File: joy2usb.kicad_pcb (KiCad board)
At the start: 2 copper layers, 55 x 90 mm, 18 parts, among them J1 DB9_Male, J2 Conn_02x04_Odd_Even, SW1 RST, SW2 SW_SPDT, U1 Arduino_Pro_Micro, U2 4066

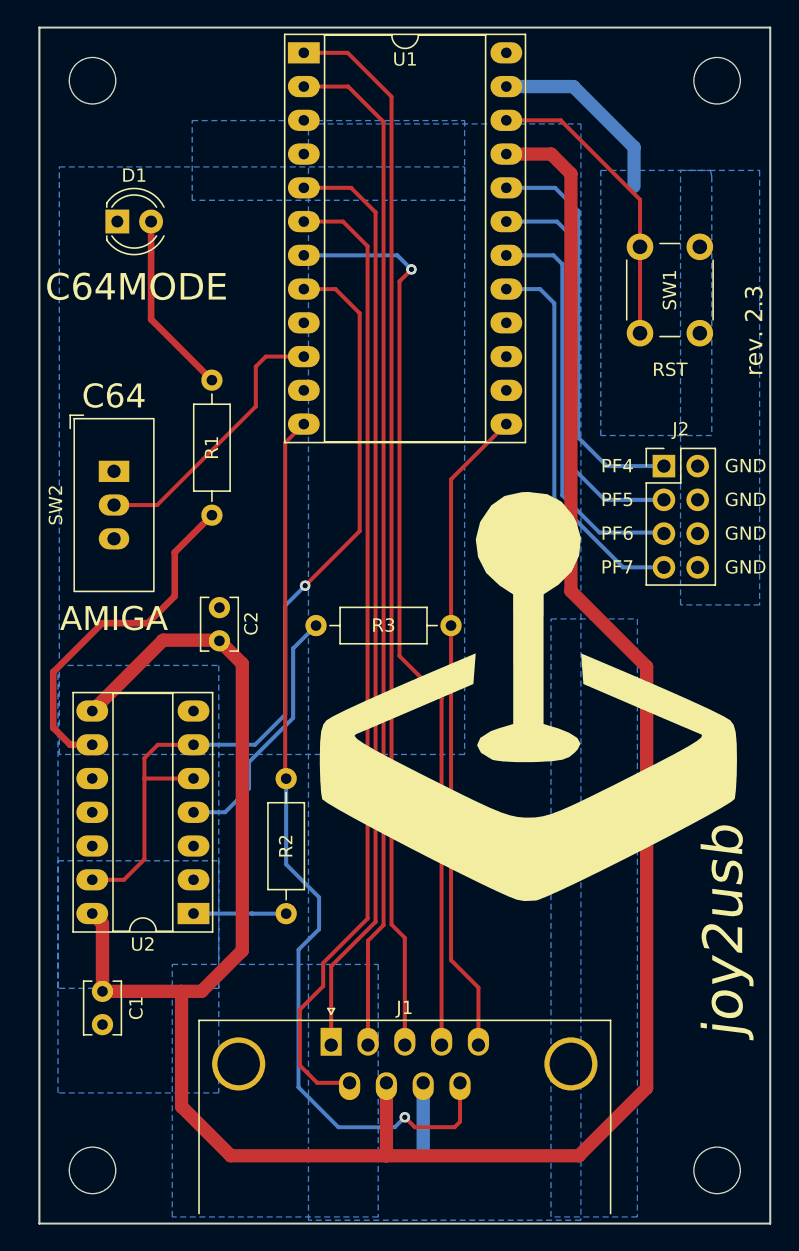
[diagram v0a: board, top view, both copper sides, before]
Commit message: PCB Rev. 2.4
update: rounded corners
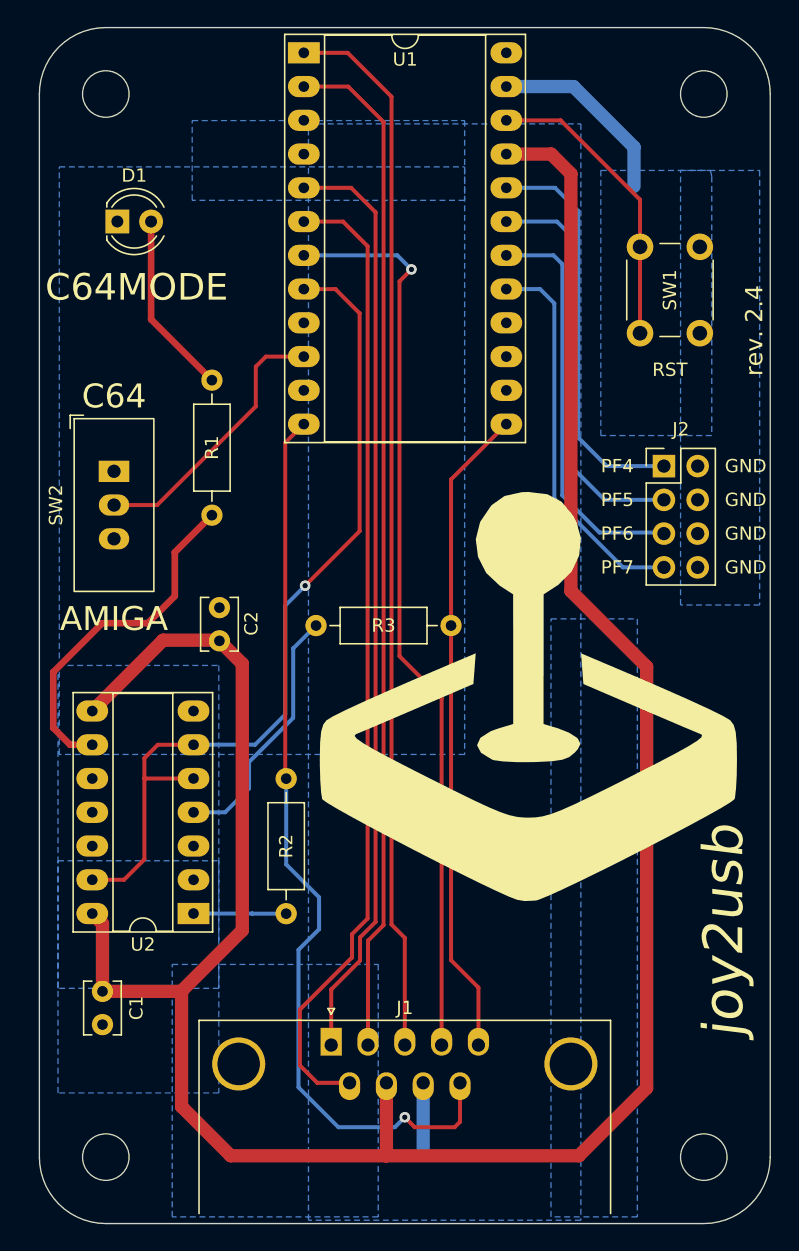
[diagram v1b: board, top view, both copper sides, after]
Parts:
- moved H1 1.41 mm to (118.0, 140.0)
- moved H2 1.41 mm to (163.0, 60.0)
- moved H3 1.41 mm to (118.0, 60.0)
- moved H4 1.41 mm to (163.0, 140.0)
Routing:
- net VCC: track 183.2 -> 182.4 mm
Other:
- outline, holes or cut-outs redrawn
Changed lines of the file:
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@@
   (title_block
     (title "joy2usb")
-    (rev "2.3")
+    (rev "2.4")
     (company "mistepien")
   )
@@
   (net 26 "unconnected-(U1-Pad3)")
   (net 27 "Net-(R1-Pad1)")
-  (net 28 "Net-(R2-Pad2)")
-  (net 29 "Net-(R3-Pad1)")
+  (net 28 "Net-(U2-Pad1)")
+  (net 29 "Net-(U2-Pad4)")
   (footprint "Resistor_THT:R_Axial_DIN0207_L6.3mm_D2.5mm_P10.16mm_Horizontal" (layer "F.Cu")
     (at 133.82 100)
@@
     (fp_line (start 8.23 -1.25) (end 1.93 -1.25) (layer "F.Fab") (width 0.1))
     (pad "1" thru_hole circle (at 0 0) (size 1.6 1.6) (drill 0.8) (layers *.Cu *.Mask)
-      (net 29 "Net-(R3-Pad1)") (pintype "passive"))
+      (net 29 "Net-(U2-Pad4)") (pintype "passive"))
     (pad "2" thru_hole oval (at 10.16 0) (size 1.6 1.6) (drill 0.8) (layers *.Cu *.Mask)
       (net 5 "/F3BTN") (pintype "passive"))
@@
       (net 9 "/F2BTN") (pintype "passive"))
     (pad "2" thru_hole oval (at 10.16 0 270) (size 1.6 1.6) (drill 0.8) (layers *.Cu *.Mask)
-      (net 28 "Net-(R2-Pad2)") (pintype "passive"))
+      (net 28 "Net-(U2-Pad1)") (pintype "passive"))
     (model "${KICAD6_3DMODEL_DIR}/Resistor_THT.3dshapes/R_Axial_DIN0207_L6.3mm_D2.5mm_P10.16mm_Horizontal.wrl"
       (offset (xyz 0 0 0))
@@
   )
   (footprint "MountingHole:MountingHole_3.5mm" (layer "F.Cu")
-    (at 164 141)
+    (at 163 140)
     (descr "Mounting Hole 3.5mm, no annular")
     (tags "mounting hole 3.5mm no annular")
@@
   )
   (footprint "MountingHole:MountingHole_3.5mm" (layer "F.Cu")
-    (at 164 59)
+    (at 163 60)
     (descr "Mounting Hole 3.5mm, no annular")
     (tags "mounting hole 3.5mm no annular")
@@
     (fp_line (start 1.635 -1.27) (end 6.985 -1.27) (layer "F.Fab") (width 0.1))
     (pad "1" thru_hole rect (at 0 0 180) (size 2.4 1.6) (drill 0.8) (layers *.Cu *.Mask)
-      (net 28 "Net-(R2-Pad2)") (pintype "passive"))
+      (net 28 "Net-(U2-Pad1)") (pintype "passive"))
     (pad "2" thru_hole oval (at 0 2.54 180) (size 2.4 1.6) (drill 0.8) (layers *.Cu *.Mask)
       (net 8 "GND1") (pintype "passive"))
@@
       (net 8 "GND1") (pintype "passive"))
     (pad "4" thru_hole oval (at 0 7.62 180) (size 2.4 1.6) (drill 0.8) (layers *.Cu *.Mask)
-      (net 29 "Net-(R3-Pad1)") (pintype "passive"))
+      (net 29 "Net-(U2-Pad4)") (pintype "passive"))
     (pad "5" thru_hole oval (at 0 10.16 180) (size 2.4 1.6) (drill 0.8) (layers *.Cu *.Mask)
       (net 24 "/F2F3MODE") (pintype "input"))
@@
   )
   (footprint "MountingHole:MountingHole_3.5mm" (layer "F.Cu")
-    (at 117 59)
+    (at 118 60)
     (descr "Mounting Hole 3.5mm, no annular")
     (tags "mounting hole 3.5mm no annular")
@@
   )
   (footprint "MountingHole:MountingHole_3.5mm" (layer "F.Cu")
-    (at 117 141)
+    (at 118 140)
     (descr "Mounting Hole 3.5mm, no annular")
     (tags "mounting hole 3.5mm no annular")
@@
       ) (layer "B.SilkS") (width 0.01) (fill solid))
   )
-  (gr_rect (start 113 55) (end 168 145) (layer "Edge.Cuts") (width 0.15) (fill none))
+  (gr_line (start 163 55) (end 118 55) (layer "Edge.Cuts") (width 0.1))
+  (gr_line (start 118 145) (end 163 145) (layer "Edge.Cuts") (width 0.1))
+  (gr_arc (start 163 55) (mid 166.535534 56.464466) (end 168 60) (layer "Edge.Cuts") (width 0.1))
+  (gr_arc (start 113 60) (mid 114.464466 56.464466) (end 118 55) (layer "Edge.Cuts") (width 0.1))
+  (gr_line (start 168 140) (end 168 60) (layer "Edge.Cuts") (width 0.1))
+  (gr_arc (start 168 140) (mid 166.535534 143.535534) (end 163 145) (layer "Edge.Cuts") (width 0.1))
+  (gr_arc (start 118 145) (mid 114.464466 143.535534) (end 113 140) (layer "Edge.Cuts") (width 0.1))
+  (gr_line (start 113 60) (end 113 140) (layer "Edge.Cuts") (width 0.1))
   (gr_text "rev. ${REVISION}" (at 166.8 71.5 -90) (layer "B.SilkS")
     (effects (font (size 1.3 1.3) (thickness 0.3)) (justify mirror))
@@
   )
   (dimension (type aligned) (layer "Dwgs.User")
-    (pts (xy 164 141) (xy 164 59))
+    (pts (xy 163 140) (xy 163 60))
     (height 22.5)
-    (gr_text "82.0000 mm" (at 185.35 100 90) (layer "Dwgs.User")
+    (gr_text "80.0000 mm" (at 184.35 100 90) (layer "Dwgs.User")
       (effects (font (size 1 1) (thickness 0.15)))
     )
@@
   )
   (dimension (type aligned) (layer "Dwgs.User")
-    (pts (xy 117 59) (xy 164 59))
+    (pts (xy 118 60) (xy 163 60))
     (height -27)
-    (gr_text "47.0000 mm" (at 140.5 30.85) (layer "Dwgs.User")
+    (gr_text "45.0000 mm" (at 140.5 31.85) (layer "Dwgs.User")
       (effects (font (size 1 1) (thickness 0.15)))
     )
@@
   )
   (dimension (type aligned) (layer "Dwgs.User")
-    (pts (xy 113 55) (xy 168 55))
-    (height -13.8)
-    (gr_text "55.0000 mm" (at 140.5 40.05) (layer "Dwgs.User")
+    (pts (xy 113 60) (xy 168 60))
+    (height -20)
+    (gr_text "55.0000 mm" (at 140.5 38.85) (layer "Dwgs.User")
       (effects (font (size 1 1) (thickness 0.15)))
     )
@@
   )
   (dimension (type aligned) (layer "Dwgs.User")
-    (pts (xy 168 55) (xy 168 145))
-    (height -6.5)
-    (gr_text "90.0000 mm" (at 173.35 100 90) (layer "Dwgs.User")
+    (pts (xy 163 55) (xy 163 145))
+    (height -16)
+    (gr_text "90.0000 mm" (at 177.85 100 90) (layer "Dwgs.User")
       (effects (font (size 1 1) (thickness 0.15)))
     )
@@
     (style (thickness 0.15) (arrow_length 1.27) (text_position_mode 0) (extension_height 0.58642) (extension_offset 0.5) keep_text_aligned)
   )
+  (segment (start 136.46 67.06) (end 138.3 68.9) (width 0.3) (layer "F.Cu") (net 1))
+  (segment (start 137.13 125.218528) (end 134.96 127.388528) (width 0.3) (layer "F.Cu") (net 1))
   (segment (start 132.9 67.06) (end 136.46 67.06) (width 0.3) (layer "F.Cu") (net 1))
-  (segment (start 136.46 67.06) (end 138.3 68.9) (width 0.3) (layer "F.Cu") (net 1))
-  (segment (start 134.96 125.638528) (end 134.96 131.569669) (width 0.3) (layer "F.Cu") (net 1))
-  (segment (start 138.3 122.298528) (end 134.96 125.638528) (width 0.3) (layer "F.Cu") (net 1))
   (segment (start 138.3 68.9) (end 138.3 122.298528) (width 0.3) (layer "F.Cu") (net 1))
+  (segment (start 134.96 127.388528) (end 134.96 131.569669) (width 0.3) (layer "F.Cu") (net 1))
+  (segment (start 137.13 123.468528) (end 137.13 125.218528) (width 0.3) (layer "F.Cu") (net 1))
+  (segment (start 138.3 122.298528) (end 137.13 123.468528) (width 0.3) (layer "F.Cu") (net 1))
   (segment (start 132.9 59.44) (end 136.24 59.44) (width 0.3) (layer "F.Cu") (net 2))
   (segment (start 137.73 123.717056) (end 137.73 131.569669) (width 0.3) (layer "F.Cu") (net 2))
@@
   (segment (start 146.04 127.24) (end 146.04 131.569669) (width 0.3) (layer "F.Cu") (net 5))
   (segment (start 143.98 100) (end 143.98 125.18) (width 0.3) (layer "F.Cu") (net 5))
+  (segment (start 136.53 124.97) (end 132.6 128.9) (width 0.3) (layer "F.Cu") (net 6))
+  (segment (start 137.7 122.05) (end 136.53 123.22) (width 0.3) (layer "F.Cu") (net 6))
+  (segment (start 136.53 123.22) (end 136.53 124.97) (width 0.3) (layer "F.Cu") (net 6))
   (segment (start 137.7 71.45) (end 137.7 122.05) (width 0.3) (layer "F.Cu") (net 6))
-  (segment (start 137.7 122.05) (end 134.36 125.39) (width 0.3) (layer "F.Cu") (net 6))
-  (segment (start 135.85 69.6) (end 137.7 71.45) (width 0.3) (layer "F.Cu") (net 6))
-  (segment (start 134.36 127.14) (end 132.6 128.9) (width 0.3) (layer "F.Cu") (net 6))
+  (segment (start 133.909669 134.409669) (end 136.345 134.409669) (width 0.3) (layer "F.Cu") (net 6))
+  (segment (start 132.6 133.1) (end 133.909669 134.409669) (width 0.3) (layer "F.Cu") (net 6))
   (segment (start 132.6 128.9) (end 132.6 133.1) (width 0.3) (layer "F.Cu") (net 6))
   (segment (start 132.9 69.6) (end 135.85 69.6) (width 0.3) (layer "F.Cu") (net 6))
-  (segment (start 132.6 133.1) (end 133.909669 134.409669) (width 0.3) (layer "F.Cu") (net 6))
-  (segment (start 134.36 125.39) (end 134.36 127.14) (width 0.3) (layer "F.Cu") (net 6))
-  (segment (start 133.909669 134.409669) (end 136.345 134.409669) (width 0.3) (layer "F.Cu") (net 6))
-  (segment (start 128.27 124.46) (end 125.202 127.528) (width 1) (layer "F.Cu") (net 7))
+  (segment (start 135.85 69.6) (end 137.7 71.45) (width 0.3) (layer "F.Cu") (net 6))
   (segment (start 158.7 134.8) (end 153.6 139.9) (width 1) (layer "F.Cu") (net 7))
   (segment (start 123.7 136.2) (end 127.4 139.9) (width 1) (layer "F.Cu") (net 7))
   (segment (start 117.75 127.528) (end 117.75 122.441) (width 1) (layer "F.Cu") (net 7))
-  (segment (start 122.311 101.1) (end 126.5 101.1) (width 1) (layer "F.Cu") (net 7))
   (segment (start 117.75 122.441) (end 116.98 121.671) (width 1) (layer "F.Cu") (net 7))
   (segment (start 158.7 103.1) (end 158.7 134.8) (width 1) (layer "F.Cu") (net 7))
+  (segment (start 122.311 101.1) (end 126.5 101.1) (width 1) (layer "F.Cu") (net 7))
   (segment (start 126.5 101.1) (end 128.27 102.87) (width 1) (layer "F.Cu") (net 7))
   (segment (start 139.115 139.885) (end 139.1 139.9) (width 1) (layer "F.Cu") (net 7))
@@
   (segment (start 139.115 134.409669) (end 139.115 139.885) (width 1) (layer "F.Cu") (net 7))
   (segment (start 123.7 136.2) (end 123.7 127.55) (width 1) (layer "F.Cu") (net 7))
-  (segment (start 128.27 102.87) (end 128.27 124.46) (width 1) (layer "F.Cu") (net 7))
+  (segment (start 128.27 122.936) (end 123.678 127.528) (width 1) (layer "F.Cu") (net 7))
   (segment (start 153 66) (end 153 97.4) (width 1) (layer "F.Cu") (net 7))
   (segment (start 117.75 127.528) (end 123.678 127.528) (width 1) (layer "F.Cu") (net 7))
   (segment (start 153.6 139.9) (end 139.1 139.9) (width 1) (layer "F.Cu") (net 7))
-  (segment (start 125.202 127.528) (end 123.678 127.528) (width 1) (layer "F.Cu") (net 7))
   (segment (start 127.4 139.9) (end 139.1 139.9) (width 1) (layer "F.Cu") (net 7))
+  (segment (start 128.27 102.87) (end 128.27 122.936) (width 1) (layer "F.Cu") (net 7))
   (segment (start 123.7 127.55) (end 123.678 127.528) (width 1) (layer "F.Cu") (net 7))
   (segment (start 151.52 64.52) (end 153 66) (width 1) (layer "F.Cu") (net 7))

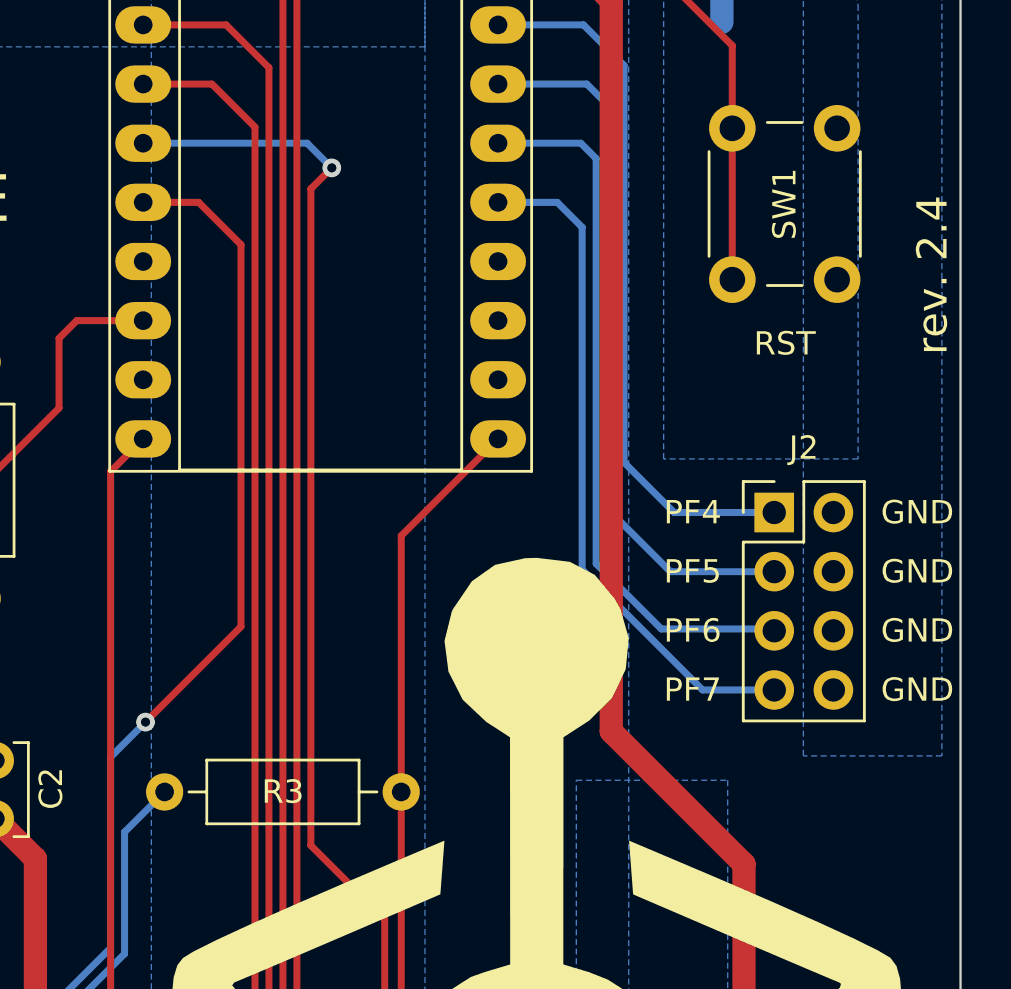
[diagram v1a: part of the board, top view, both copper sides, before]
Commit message: PCB Rev. 2.41
fix: update of nets
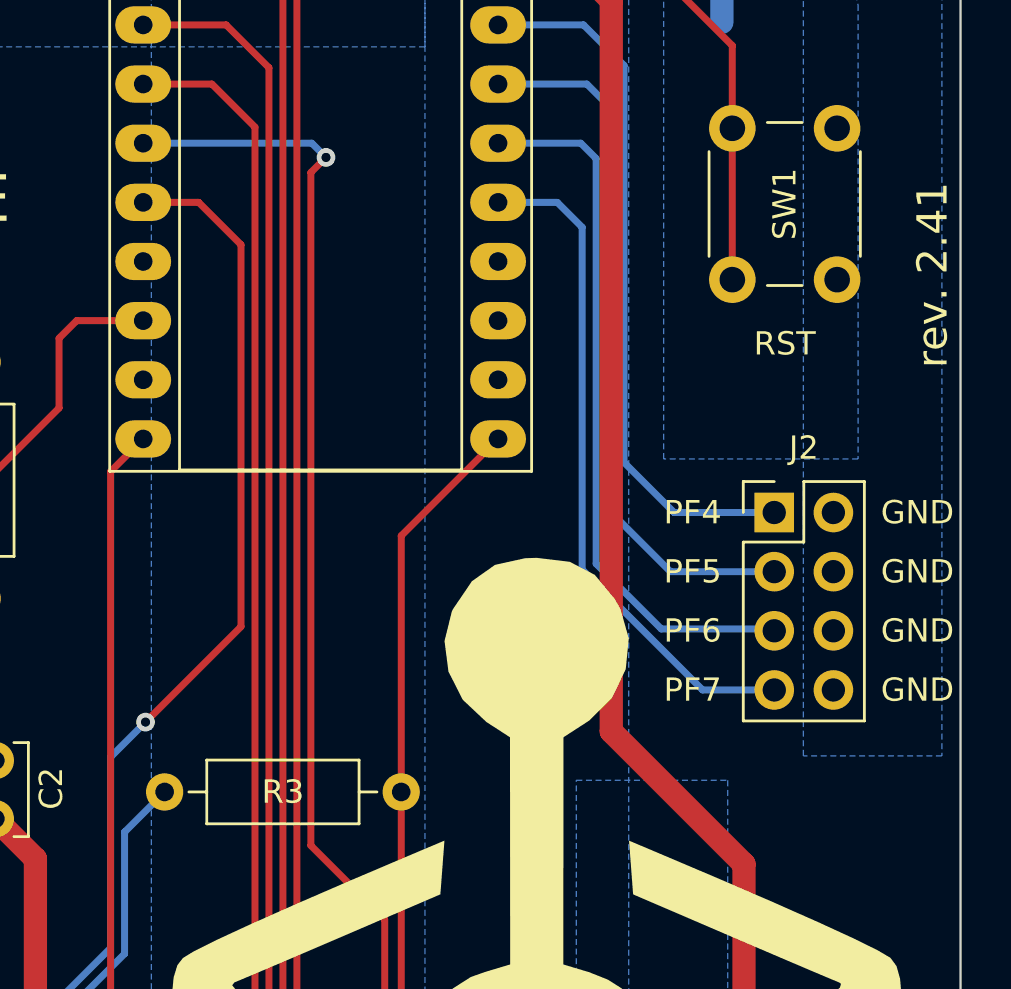
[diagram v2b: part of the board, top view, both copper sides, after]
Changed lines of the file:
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@@
   (title_block
     (title "joy2usb")
-    (rev "2.4")
+    (rev "2.41")
     (company "mistepien")
   )
@@
   (net 26 "unconnected-(U1-Pad3)")
   (net 27 "Net-(R1-Pad1)")
-  (net 28 "Net-(U2-Pad1)")
-  (net 29 "Net-(U2-Pad4)")
+  (net 28 "Net-(R2-Pad2)")
+  (net 29 "Net-(R3-Pad1)")
   (footprint "Resistor_THT:R_Axial_DIN0207_L6.3mm_D2.5mm_P10.16mm_Horizontal" (layer "F.Cu")
     (at 133.82 100)
@@
     (fp_line (start 8.23 -1.25) (end 1.93 -1.25) (layer "F.Fab") (width 0.1))
     (pad "1" thru_hole circle (at 0 0) (size 1.6 1.6) (drill 0.8) (layers *.Cu *.Mask)
-      (net 29 "Net-(U2-Pad4)") (pintype "passive"))
+      (net 29 "Net-(R3-Pad1)") (pintype "passive"))
     (pad "2" thru_hole oval (at 10.16 0) (size 1.6 1.6) (drill 0.8) (layers *.Cu *.Mask)
       (net 5 "/F3BTN") (pintype "passive"))
@@
       (net 9 "/F2BTN") (pintype "passive"))
     (pad "2" thru_hole oval (at 10.16 0 270) (size 1.6 1.6) (drill 0.8) (layers *.Cu *.Mask)
-      (net 28 "Net-(U2-Pad1)") (pintype "passive"))
+      (net 28 "Net-(R2-Pad2)") (pintype "passive"))
     (model "${KICAD6_3DMODEL_DIR}/Resistor_THT.3dshapes/R_Axial_DIN0207_L6.3mm_D2.5mm_P10.16mm_Horizontal.wrl"
       (offset (xyz 0 0 0))
@@
     (fp_line (start 1.635 -1.27) (end 6.985 -1.27) (layer "F.Fab") (width 0.1))
     (pad "1" thru_hole rect (at 0 0 180) (size 2.4 1.6) (drill 0.8) (layers *.Cu *.Mask)
-      (net 28 "Net-(U2-Pad1)") (pintype "passive"))
+      (net 28 "Net-(R2-Pad2)") (pintype "passive"))
     (pad "2" thru_hole oval (at 0 2.54 180) (size 2.4 1.6) (drill 0.8) (layers *.Cu *.Mask)
       (net 8 "GND1") (pintype "passive"))
@@
       (net 8 "GND1") (pintype "passive"))
     (pad "4" thru_hole oval (at 0 7.62 180) (size 2.4 1.6) (drill 0.8) (layers *.Cu *.Mask)
-      (net 29 "Net-(U2-Pad4)") (pintype "passive"))
+      (net 29 "Net-(R3-Pad1)") (pintype "passive"))
     (pad "5" thru_hole oval (at 0 10.16 180) (size 2.4 1.6) (drill 0.8) (layers *.Cu *.Mask)
       (net 24 "/F2F3MODE") (pintype "input"))
@@
   (segment (start 132.9 56.9) (end 136.2 56.9) (width 0.3) (layer "F.Cu") (net 3))
   (segment (start 140.5 123.5) (end 140.5 131.569669) (width 0.3) (layer "F.Cu") (net 3))
+  (segment (start 140.75 72.75) (end 140.1 73.4) (width 0.3) (layer "F.Cu") (net 4))
   (segment (start 140.1 102.3) (end 143.27 105.47) (width 0.3) (layer "F.Cu") (net 4))
-  (segment (start 140.1 74.1) (end 140.1 102.3) (width 0.3) (layer "F.Cu") (net 4))
-  (segment (start 141 73.2) (end 140.1 74.1) (width 0.3) (layer "F.Cu") (net 4))
   (segment (start 143.27 105.47) (end 143.27 131.569669) (width 0.3) (layer "F.Cu") (net 4))
-  (via (at 141 73.2) (size 0.8) (drill 0.4) (layers "F.Cu" "B.Cu") (net 4))
-  (segment (start 141 73.2) (end 139.94 72.14) (width 0.3) (layer "B.Cu") (net 4))
-  (segment (start 139.94 72.14) (end 132.9 72.14) (width 0.3) (layer "B.Cu") (net 4))
+  (segment (start 140.1 73.4) (end 140.1 102.3) (width 0.3) (layer "F.Cu") (net 4))
+  (via (at 140.75 72.75) (size 0.8) (drill 0.4) (layers "F.Cu" "B.Cu") (net 4))
+  (segment (start 140.14 72.14) (end 132.9 72.14) (width 0.3) (layer "B.Cu") (net 4))
+  (segment (start 140.75 72.75) (end 140.14 72.14) (width 0.3) (layer "B.Cu") (net 4))
   (segment (start 143.98 125.18) (end 146.04 127.24) (width 0.3) (layer "F.Cu") (net 5))
   (segment (start 148.14 84.84) (end 143.98 89) (width 0.3) (layer "F.Cu") (net 5))
